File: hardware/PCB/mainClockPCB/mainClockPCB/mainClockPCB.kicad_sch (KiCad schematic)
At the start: 61 parts, among them IC1 TMP275AIDR, IC2 SPX1117M3-L_TR, IC3 MCP7940N-I_P, IC4 PAM8904QJER, J1 USB_C_Receptacle_USB2.0_16P, J2 Conn_01x09_Socket, J3 Conn_01x02_Socket, J4 Conn_01x08, J5 Conn_01x09, J6 Conn_01x09, J7 Conn_01x05, J8 Conn_01x06, J9 Conn_01x05, SW1 SW_Push, SW2 SW_Push, U1 PEC11R-4320K-S0012, U2 USBLC6-2SC6, U3 ESP32-S3-WROOM-2, U4 74HC165, Y1 AB26T-32.768KHZ-6

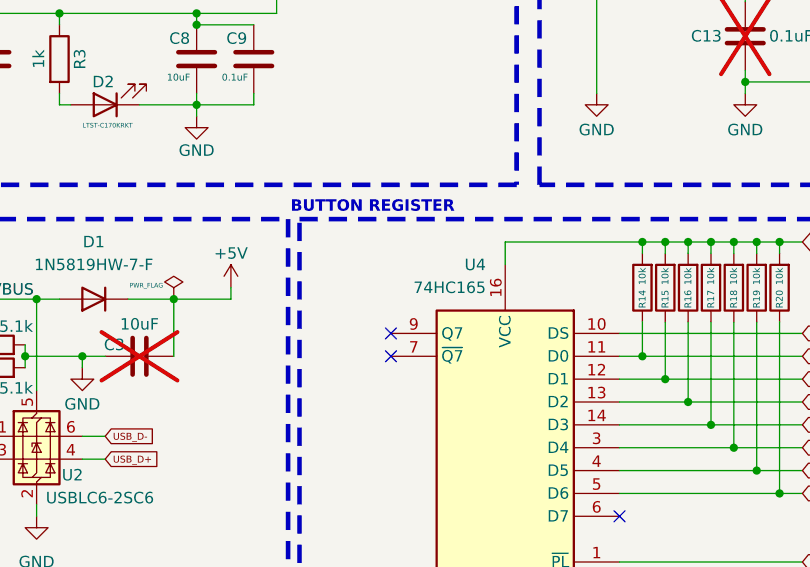
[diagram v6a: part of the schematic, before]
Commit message: bypass cap on PISO S
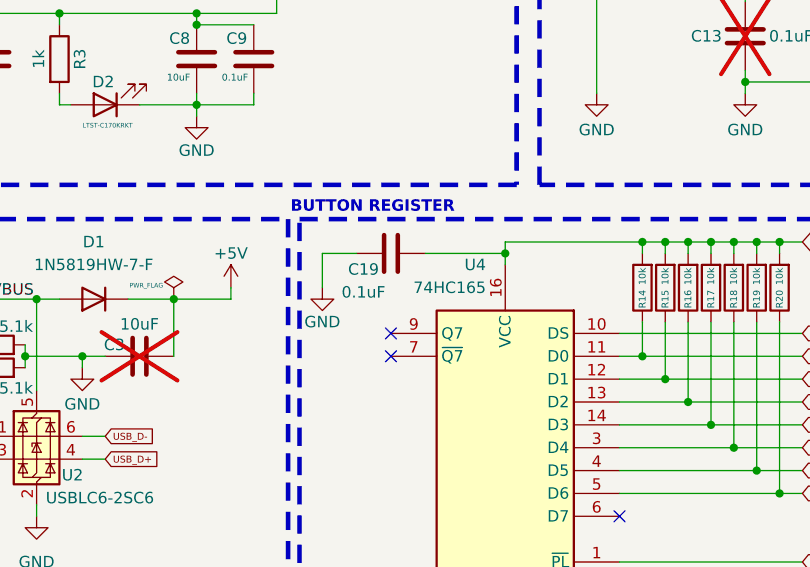
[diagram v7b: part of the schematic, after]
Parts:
- added C19: 0.1uF, Capacitor_SMD:C_0603_1608Metric_Pad1.08x0.95mm_HandSolder, symbol Device:C
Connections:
- net ESP_3v3: now also C19.2
- net GND: now also C19.1
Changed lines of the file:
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@@
 	)
 	(junction
+		(at 106.68 139.7)
+		(diameter 0)
+		(color 0 0 0 0)
+	)
+	(junction
 		(at 213.36 147.32)
 		(diameter 0)
@@
 	(wire
 		(pts
+			(xy 106.68 139.7) (xy 106.68 138.43)
+		)
+		(stroke
+			(width 0)
+			(type default)
+		)
+	)
+	(wire
+		(pts
 			(xy 158.75 104.14) (xy 161.29 104.14)
 		)
@@
 	(wire
 		(pts
+			(xy 97.79 139.7) (xy 106.68 139.7)
+		)
+		(stroke
+			(width 0)
+			(type default)
+		)
+	)
+	(wire
+		(pts
 			(xy 214.63 139.7) (xy 215.9 139.7)
 		)
@@
 	(wire
 		(pts
-			(xy 106.68 140.97) (xy 106.68 138.43)
+			(xy 106.68 140.97) (xy 106.68 139.7)
 		)
 		(stroke
@@
 	(wire
 		(pts
+			(xy 86.36 139.7) (xy 86.36 143.51)
+		)
+		(stroke
+			(width 0)
+			(type default)
+		)
+	)
+	(wire
+		(pts
 			(xy 119.38 156.21) (xy 127 156.21)
 		)
@@
 	(wire
 		(pts
+			(xy 90.17 139.7) (xy 86.36 139.7)
+		)
+		(stroke
+			(width 0)
+			(type default)
+		)
+	)
+	(wire
+		(pts
 			(xy 43.18 124.46) (xy 43.18 123.19)
 		)
@@
 	(symbol
 		(lib_id "power:GND")
+		(at 86.36 143.51 0)
+		(unit 1)
+		(exclude_from_sim no)
+		(in_bom yes)
+		(on_board yes)
+		(dnp no)
+		(property "Reference" "#PWR036"
+			(at 86.36 149.86 0)
+			(effects
+				(font
+					(size 1.27 1.27)
+				)
+				(hide yes)
+			)
+		)
+		(property "Value" "GND"
+			(at 86.36 147.32 0)
+			(effects
+				(font
+					(size 1.27 1.27)
+				)
+			)
+		)
+		(property "Footprint" ""
+			(at 86.36 143.51 0)
+			(effects
+				(font
+					(size 1.27 1.27)
+				)
+				(hide yes)
+			)
+		)
+		(property "Datasheet" ""
+			(at 86.36 143.51 0)
+			(effects
+				(font
+					(size 1.27 1.27)
+				)
+				(hide yes)
+			)
+		)
+		(property "Description" "Power symbol creates a global label with name \"GND\" , ground"
+			(at 86.36 143.51 0)
+			(effects
+				(font
+					(size 1.27 1.27)
+				)
+				(hide yes)
+			)
+		)
+		(pin "1"
+		)
+		(instances
+			(project ""
+				(path "/cd91d451-ff7b-4e2a-9e6d-1f78d74b6c34"
+					(reference "#PWR036")
+					(unit 1)
+				)
+			)
+		)
+	)
+	(symbol
+		(lib_id "power:GND")
 		(at 152.4 121.92 0)
 		(unit 1)
@@
 					(unit 1)
 				)
+			)
+		)
+	)
+	(symbol
+		(lib_id "Device:C")
+		(at 93.98 139.7 90)
+		(unit 1)
+		(exclude_from_sim no)
+		(in_bom yes)
+		(on_board yes)
+		(dnp no)
+		(property "Reference" "C19"
+			(at 90.932 141.478 90)
+			(effects
+				(font
+					(size 1.27 1.27)
+				)
+			)
+		)
+		(property "Value" "0.1uF"
+			(at 90.932 144.018 90)
+			(effects
+				(font
+					(size 1.27 1.27)
+				)
+			)
+		)
+		(property "Footprint" "Capacitor_SMD:C_0603_1608Metric_Pad1.08x0.95mm_HandSolder"
+			(at 97.79 138.7348 0)
+			(effects
+				(font
+					(size 1.27 1.27)
+				)
+				(hide yes)
+			)
+		)
+		(property "Datasheet" "~"
+			(at 93.98 139.7 0)
+			(effects
+				(font
+					(size 1.27 1.27)
+				)
+				(hide yes)
+			)
+		)
+		(property "Description" "Unpolarized capacitor"
+			(at 93.98 139.7 0)
+			(effects
+				(font
+					(size 1.27 1.27)
+				)
+				(hide yes)
+			)
+		)
+		(pin "1"
+		)
+		(pin "2"
+		)
+		(instances
+			(project ""
+				(path "/cd91d451-ff7b-4e2a-9e6d-1f78d74b6c34"
+					(reference "C19")
+					(unit 1)
+				)

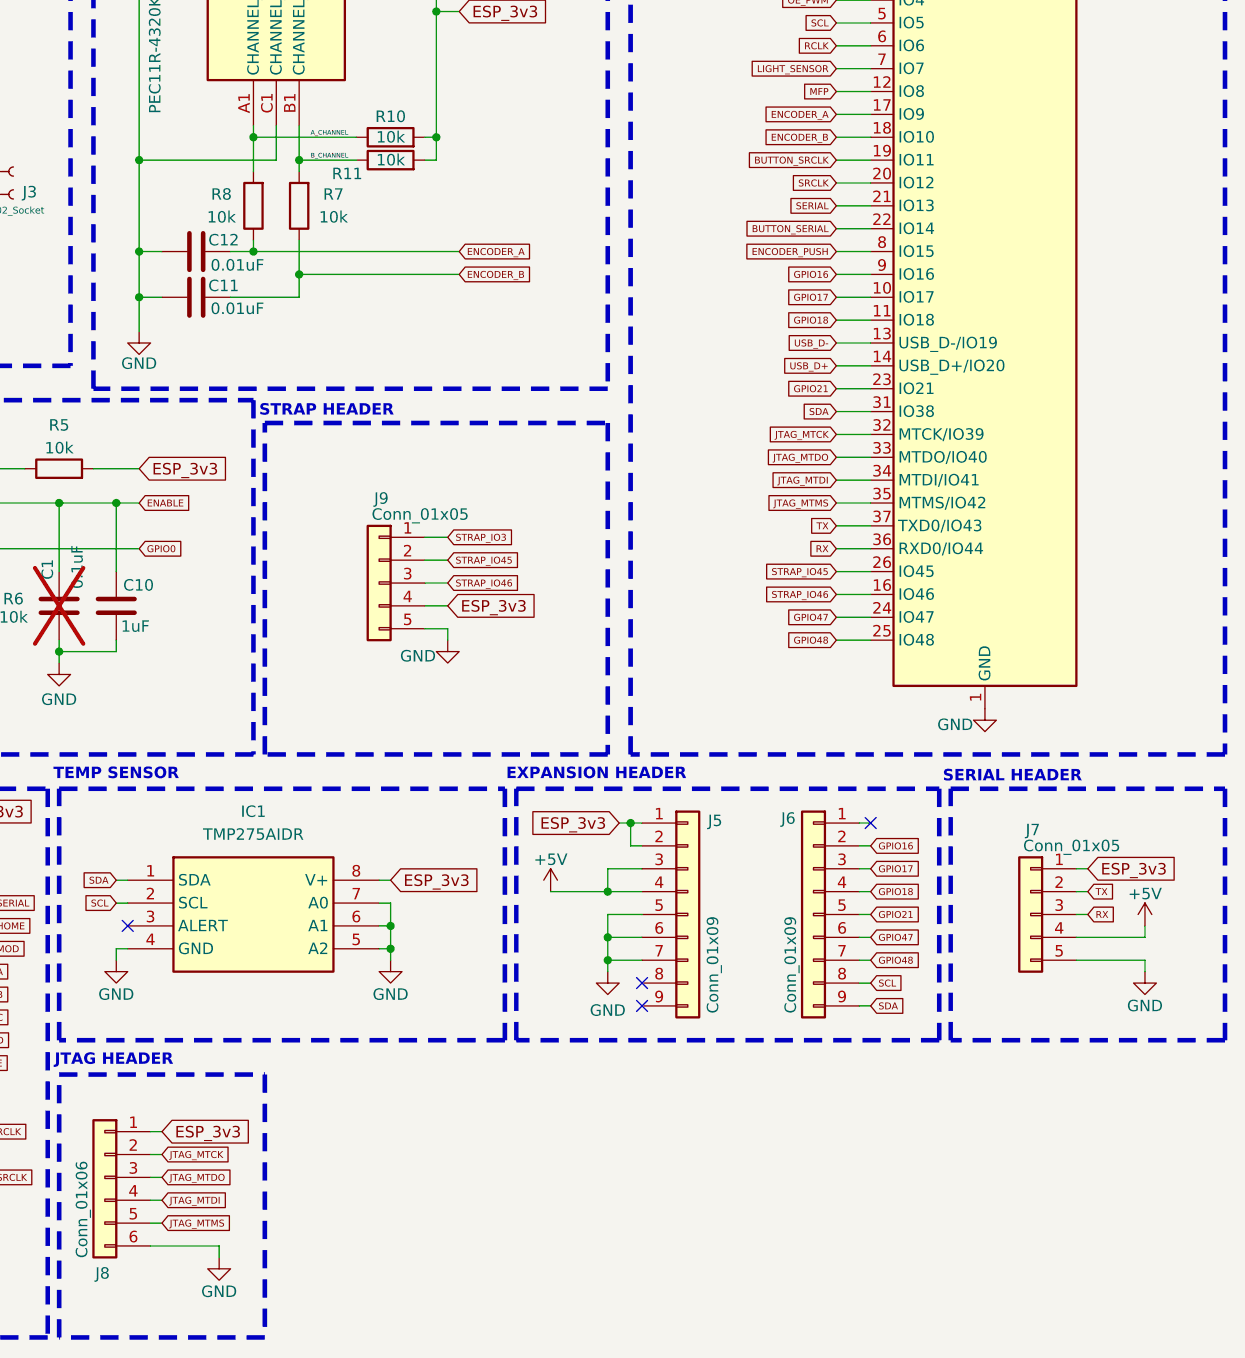
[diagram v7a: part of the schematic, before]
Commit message: Serial header on mainboard now matches FTDI standard, JTAG changed to be more standard
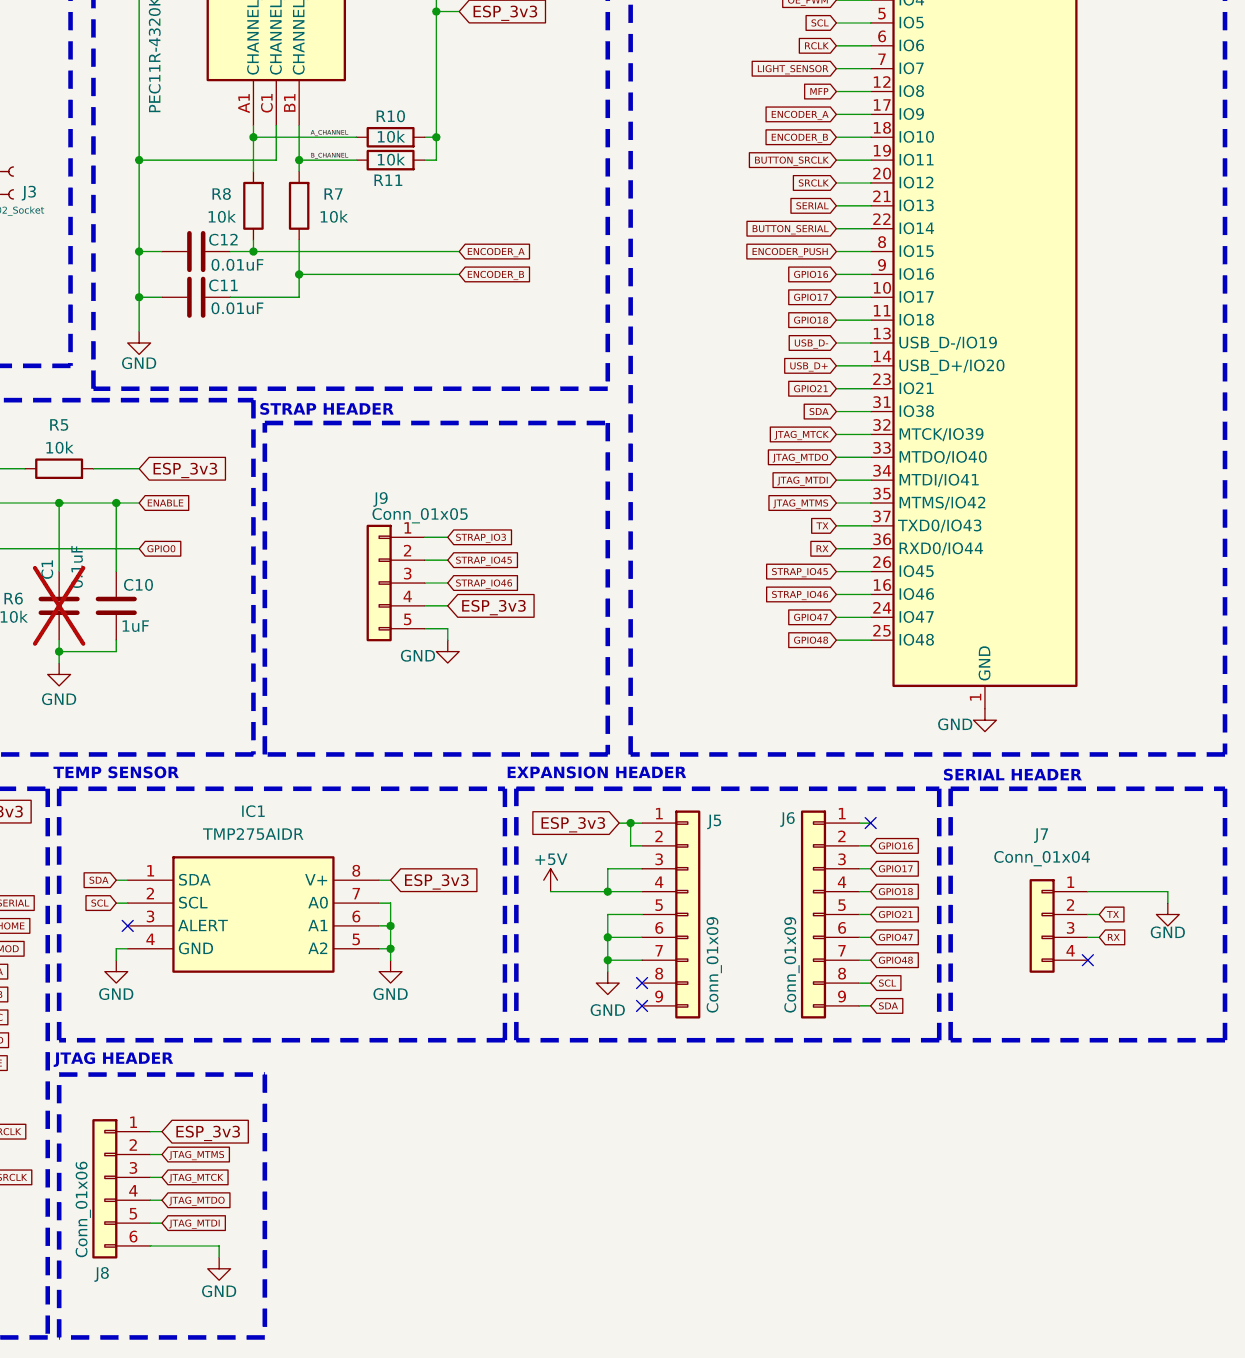
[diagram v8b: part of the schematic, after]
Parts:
- removed J7: Conn_01x05, Connector_PinSocket_2.54mm:PinSocket_1x05_P2.54mm_Vertical, symbol Connector_Generic:Conn_01x05
- added J7: Conn_01x04, symbol Connector_Generic:Conn_01x04
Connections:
- net GND: now also J7.1 (Pin_1)
- net JTAG_MTCK: now also J8.3 (Pin_3); no longer J8.2 (Pin_2)
- net JTAG_MTDI: now also J8.5 (Pin_5); no longer J8.4 (Pin_4)
- net JTAG_MTDO: now also J8.4 (Pin_4); no longer J8.3 (Pin_3)
- net JTAG_MTMS: now also J8.2 (Pin_2); no longer J8.5 (Pin_5)
- net RX: now also J7.3 (Pin_3)
- net TX: now also J7.2 (Pin_2)
- no-connect marks 13 -> 14
